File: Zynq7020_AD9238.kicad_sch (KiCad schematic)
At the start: 0 parts

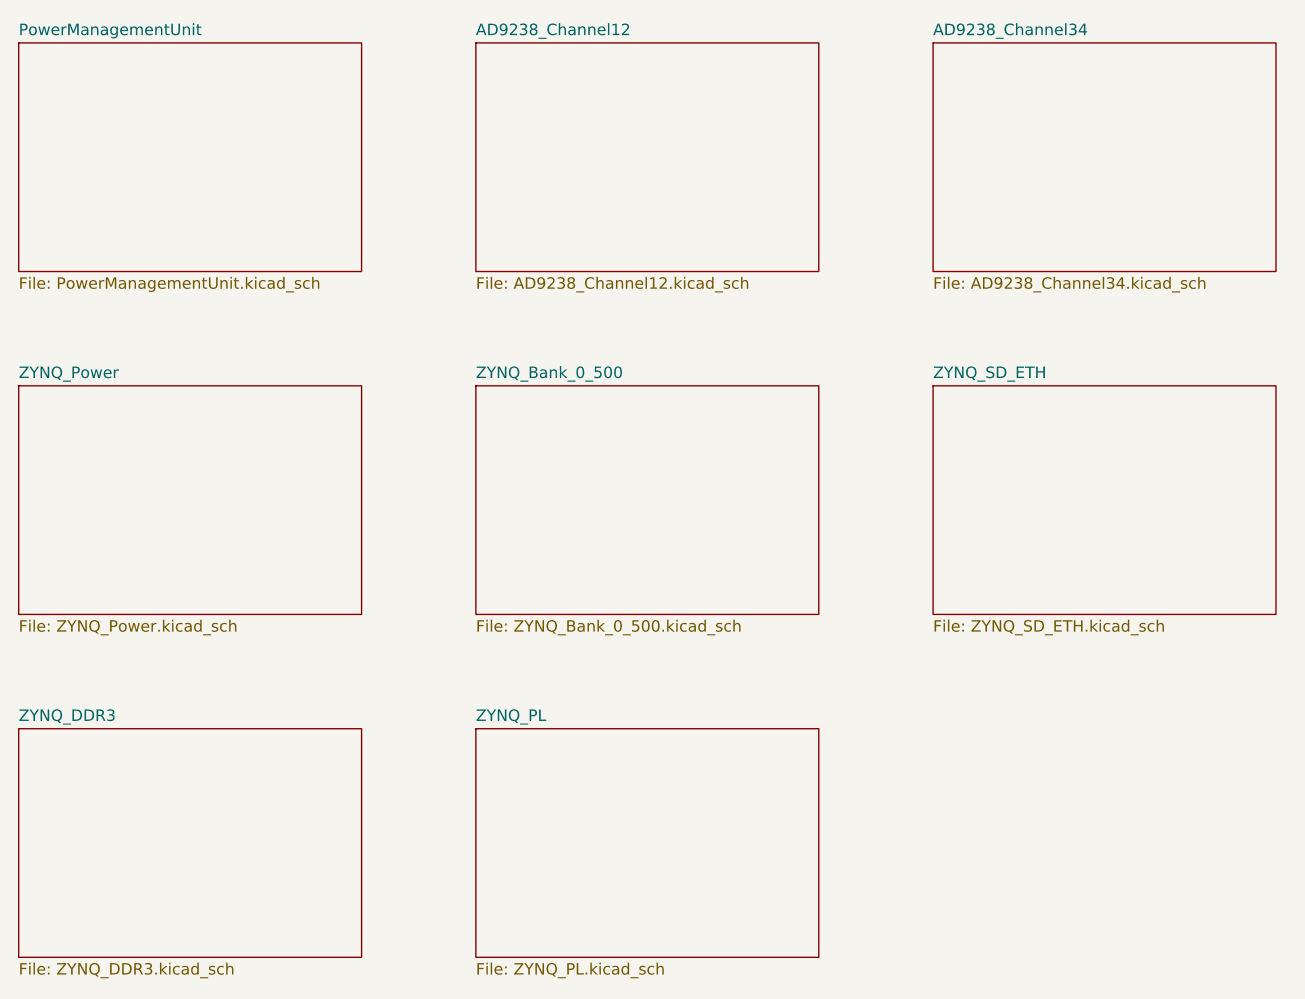
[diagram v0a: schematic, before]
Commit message: 变压器输入+两块DDR3
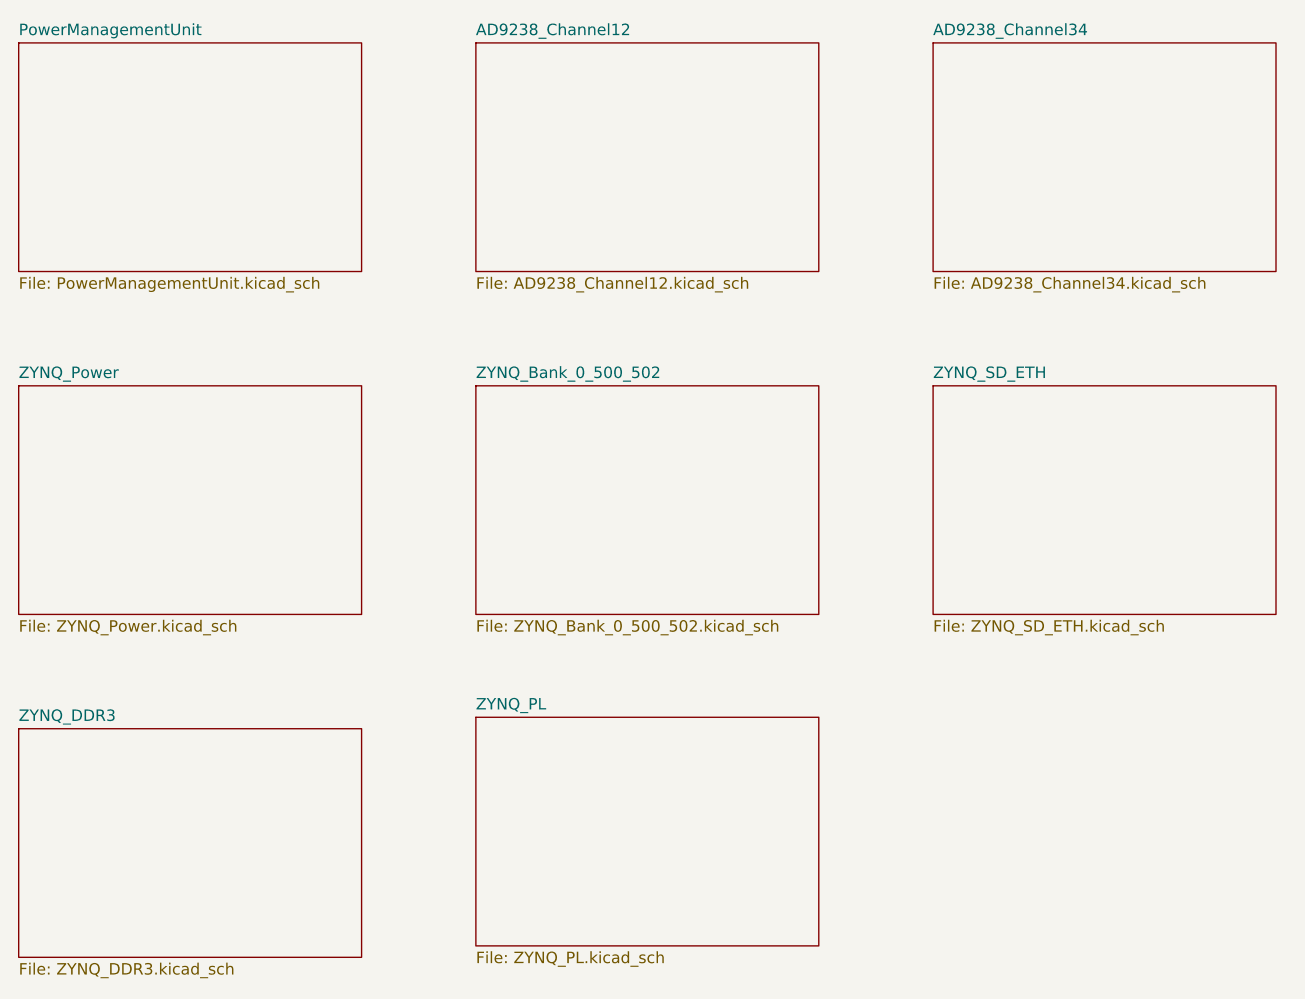
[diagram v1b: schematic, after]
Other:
- sheet ZYNQ_Bank_0_500 renamed ZYNQ_Bank_0_500_502
- sheet ZYNQ_Bank_0_500_502: file ZYNQ_Bank_0_500.kicad_sch -> ZYNQ_Bank_0_500_502.kicad_sch
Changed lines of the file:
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@@
     (instances
       (project "Zynq7020_AD9238"
-        (path "/e2c3762a-bcbe-43e8-9d28-0bac9f933799" (page "9"))
+        (path "/e2c3762a-bcbe-43e8-9d28-0bac9f933799" (page "10"))
       )
     )
@@
     )
   )
-  (sheet (at 101.6 127) (size 38.1 25.4) (fields_autoplaced)
+  (sheet (at 101.6 125.73) (size 38.1 25.4) (fields_autoplaced)
     (stroke (width 0.1524) (type solid))
     (fill (color 0 0 0 0.0000))
-    (property "Sheetname" "ZYNQ_PL" (at 101.6 126.2884 0)
+    (property "Sheetname" "ZYNQ_PL" (at 101.6 125.0184 0)
       (effects (font (size 1.27 1.27)) (justify left bottom))
     )
-    (property "Sheetfile" "ZYNQ_PL.kicad_sch" (at 101.6 152.9846 0)
+    (property "Sheetfile" "ZYNQ_PL.kicad_sch" (at 101.6 151.7146 0)
       (effects (font (size 1.27 1.27)) (justify left top))
     )
@@
     (stroke (width 0.1524) (type solid))
     (fill (color 0 0 0 0.0000))
-    (property "Sheetname" "ZYNQ_Bank_0_500" (at 101.6 88.1884 0)
+    (property "Sheetname" "ZYNQ_Bank_0_500_502" (at 101.6 88.1884 0)
       (effects (font (size 1.27 1.27)) (justify left bottom))
     )
-    (property "Sheetfile" "ZYNQ_Bank_0_500.kicad_sch" (at 101.6 114.8846 0)
+    (property "Sheetfile" "ZYNQ_Bank_0_500_502.kicad_sch" (at 101.6 114.8846 0)
       (effects (font (size 1.27 1.27)) (justify left top))
     )
